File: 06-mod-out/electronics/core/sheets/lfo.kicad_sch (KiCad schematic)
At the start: 13 parts, among them Q1 BC548C, U3 TL072

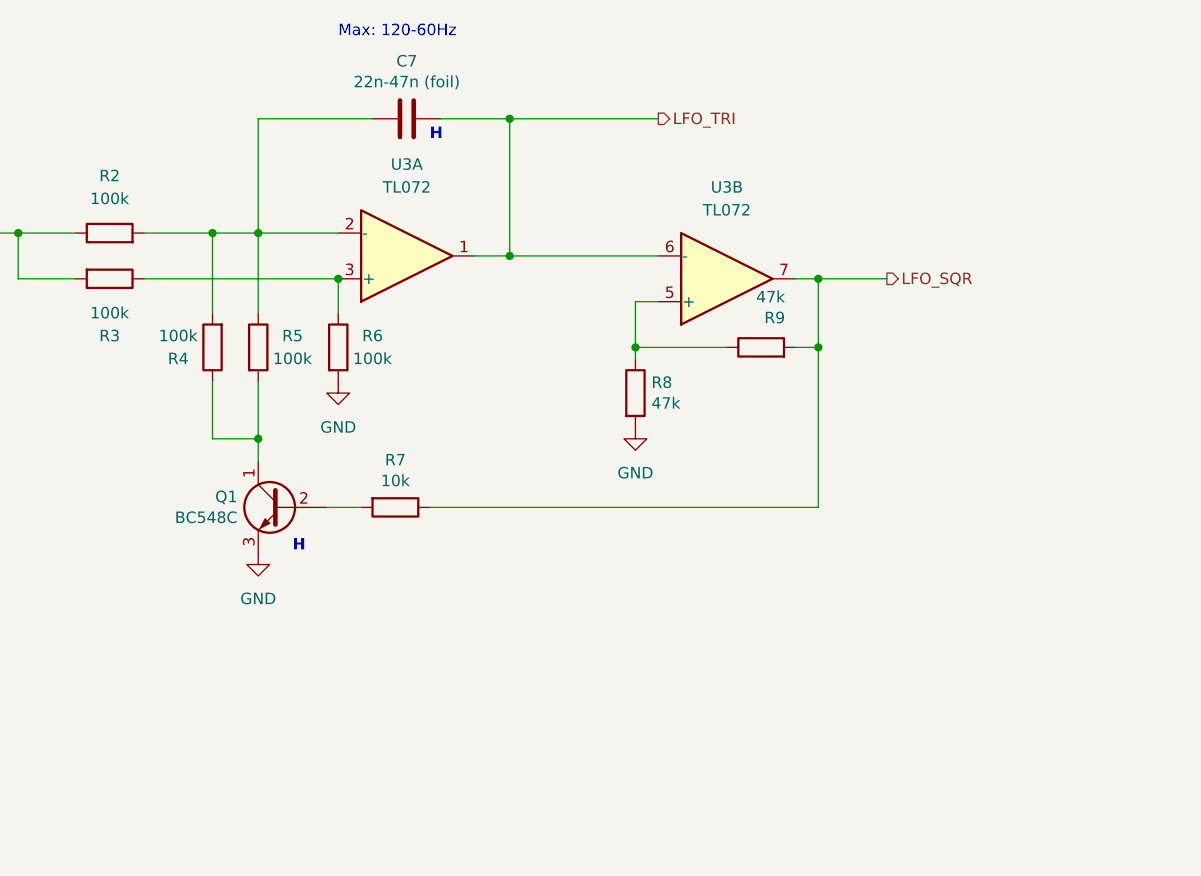
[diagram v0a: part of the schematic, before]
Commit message: Started Mod/Output PCB
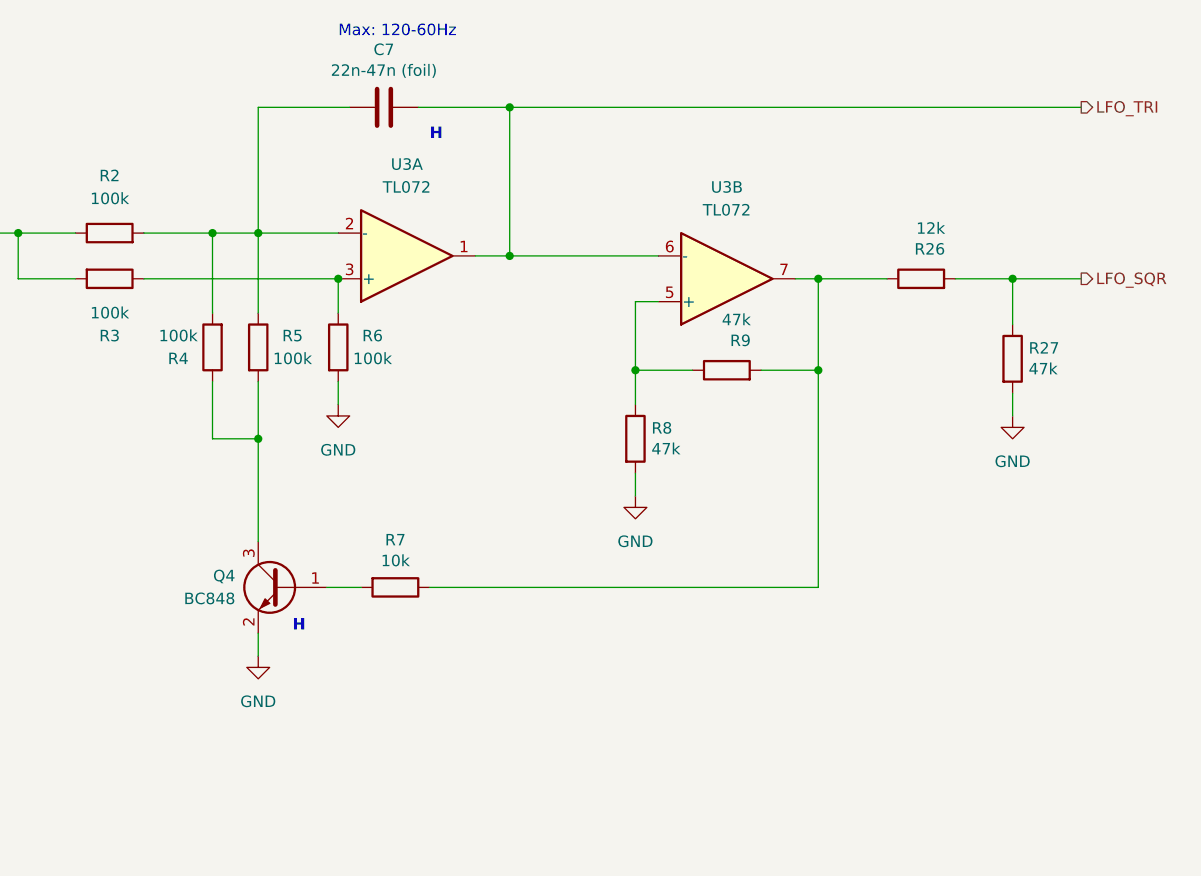
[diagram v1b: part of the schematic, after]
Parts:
- removed Q1: BC548C, Package_TO_SOT_THT:TO-92L_Inline_Wide, symbol Transistor_BJT:BC548
- added Q4: BC848, Package_TO_SOT_SMD:SOT-23, symbol Transistor_BJT:BC848
- added R26: 12k, Resistor_SMD:R_0603_1608Metric, symbol Device:R
- added R27: 47k, Resistor_SMD:R_0603_1608Metric, symbol Device:R
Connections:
- net GND: now also Q4.2 (E), R27.2
- net LFO_SQR: now also R26.2, R27.1; no longer R7.1, R9.2, U3.7
- net at R7.2: now also Q4.1 (B)
- net at R4.1, R5.2: now also Q4.3 (C)
- new net: R26.1, R7.1, R9.2, U3.7
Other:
- moved on the sheet: C7, R7, R8, R9
